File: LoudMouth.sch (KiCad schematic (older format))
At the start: 15 parts, among them P101 CONN_01X02, P102 CONN_01X02, P103 CONN_01X02, Q101 Q_NPN_BCE

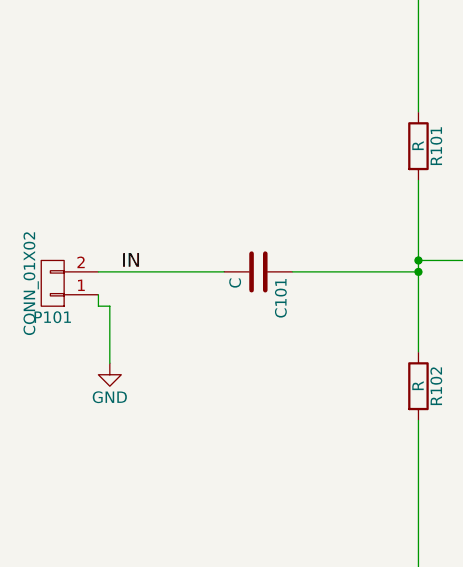
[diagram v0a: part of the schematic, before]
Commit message: Created initial layout and changed input pin config
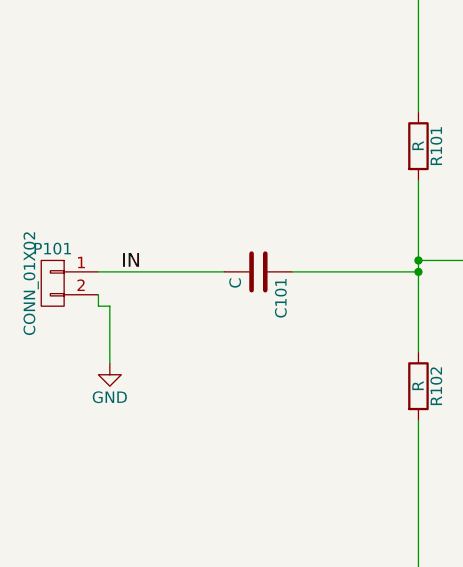
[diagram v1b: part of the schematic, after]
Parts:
- C101, C102, C103, C104: footprint (none) -> Capacitors_SMD:C_1210_HandSoldering
- P101, P102, P103: footprint (none) -> Pin_Headers:Pin_Header_Straight_1x02
- Q101: footprint (none) -> Housings_TO-92:TO-92_Molded_Narrow
- R101, R102, R103, R104, R105, R106, R107: footprint (none) -> Resistors_SMD:R_0805_HandSoldering
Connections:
- net GND: now also P101.2 (P2); no longer P101.1 (P1)
- net IN: now also P101.1 (P1); no longer P101.2 (P2)
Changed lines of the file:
@@
 F 0 "R101" V 4080 2650 50  0000 C CNN
 F 1 "R" V 4000 2650 50  0000 C CNN
-F 2 "" V 3930 2650 30  0000 C CNN
+F 2 "Resistors_SMD:R_0805_HandSoldering" V 3930 2650 30  0001 C CNN
 F 3 "" H 4000 2650 30  0000 C CNN
 	1    4000 2650
@@
 F 0 "R102" V 4080 3700 50  0000 C CNN
 F 1 "R" V 4000 3700 50  0000 C CNN
-F 2 "" V 3930 3700 30  0000 C CNN
+F 2 "Resistors_SMD:R_0805_HandSoldering" V 3930 3700 30  0001 C CNN
 F 3 "" H 4000 3700 30  0000 C CNN
 	1    4000 3700
@@
 F 0 "R104" V 5580 1500 50  0000 C CNN
 F 1 "R" V 5500 1500 50  0000 C CNN
-F 2 "" V 5430 1500 30  0000 C CNN
+F 2 "Resistors_SMD:R_0805_HandSoldering" V 5430 1500 30  0001 C CNN
 F 3 "" H 5500 1500 30  0000 C CNN
 	1    5500 1500
@@
 F 0 "R107" V 5580 4800 50  0000 C CNN
 F 1 "R" V 5500 4800 50  0000 C CNN
-F 2 "" V 5430 4800 30  0000 C CNN
+F 2 "Resistors_SMD:R_0805_HandSoldering" V 5430 4800 30  0001 C CNN
 F 3 "" H 5500 4800 30  0000 C CNN
 	1    5500 4800
@@
 F 0 "C101" H 3325 3300 50  0000 L CNN
 F 1 "C" H 3325 3100 50  0000 L CNN
-F 2 "" H 3338 3050 30  0000 C CNN
+F 2 "Capacitors_SMD:C_1210_HandSoldering" H 3338 3050 30  0001 C CNN
 F 3 "" H 3300 3200 60  0000 C CNN
 	1    3300 3200
@@
 F 0 "C104" H 6175 2400 50  0000 L CNN
 F 1 "C" H 6175 2200 50  0000 L CNN
-F 2 "" H 6188 2150 30  0000 C CNN
+F 2 "Capacitors_SMD:C_1210_HandSoldering" H 6188 2150 30  0001 C CNN
 F 3 "" H 6150 2300 60  0000 C CNN
 	1    6150 2300
@@
 F 0 "C103" H 6075 1600 50  0000 L CNN
 F 1 "C" H 6075 1400 50  0000 L CNN
-F 2 "" H 6088 1350 30  0000 C CNN
+F 2 "Capacitors_SMD:C_1210_HandSoldering" H 6088 1350 30  0001 C CNN
 F 3 "" H 6050 1500 60  0000 C CNN
 	1    6050 1500
@@
 F 0 "C102" H 5875 4900 50  0000 L CNN
 F 1 "C" H 5875 4700 50  0000 L CNN
-F 2 "" H 5888 4650 30  0000 C CNN
+F 2 "Capacitors_SMD:C_1210_HandSoldering" H 5888 4650 30  0001 C CNN
 F 3 "" H 5850 4800 60  0000 C CNN
 	1    5850 4800
@@
 F 0 "Q101" H 5700 3200 50  0000 R CNN
 F 1 "Q_NPN_BCE" H 6000 3100 50  0000 R CNN
-F 2 "" H 5600 3250 29  0000 C CNN
+F 2 "Housings_TO-92:TO-92_Molded_Narrow" H 5600 3250 29  0001 C CNN
 F 3 "" H 5400 3150 60  0000 C CNN
 	1    5400 3150
@@
 F 0 "R103" V 4930 3150 50  0000 C CNN
 F 1 "0" V 4850 3150 50  0000 C CNN
-F 2 "" V 4780 3150 30  0000 C CNN
+F 2 "Resistors_SMD:R_0805_HandSoldering" V 4780 3150 30  0001 C CNN
 F 3 "" H 4850 3150 30  0000 C CNN
 	1    4850 3150
@@
 F 0 "R106" V 5580 3750 50  0000 C CNN
 F 1 "0" V 5500 3750 50  0000 C CNN
-F 2 "" V 5430 3750 30  0000 C CNN
+F 2 "Resistors_SMD:R_0805_HandSoldering" V 5430 3750 30  0001 C CNN
 F 3 "" H 5500 3750 30  0000 C CNN
 	1    5500 3750
@@
 F 0 "R105" V 5580 2550 50  0000 C CNN
 F 1 "0" V 5500 2550 50  0000 C CNN
-F 2 "" V 5430 2550 30  0000 C CNN
+F 2 "Resistors_SMD:R_0805_HandSoldering" V 5430 2550 30  0001 C CNN
 F 3 "" H 5500 2550 30  0000 C CNN
 	1    5500 2550
@@
 F 0 "P101" H 2400 3400 50  0000 C CNN
 F 1 "CONN_01X02" V 2500 3250 50  0000 C CNN
-F 2 "" H 2400 3250 60  0000 C CNN
+F 2 "Pin_Headers:Pin_Header_Straight_1x02" H 2400 3250 60  0001 C CNN
 F 3 "" H 2400 3250 60  0000 C CNN
 	1    2400 3250
-	-1   0    0    1
+	-1   0    0    -1
 $EndComp
 $Comp
@@
 F 0 "P102" H 7100 1400 50  0000 C CNN
 F 1 "CONN_01X02" V 7200 1250 50  0000 C CNN
-F 2 "" H 7100 1250 60  0000 C CNN
+F 2 "Pin_Headers:Pin_Header_Straight_1x02" H 7100 1250 60  0001 C CNN
 F 3 "" H 7100 1250 60  0000 C CNN
 	1    7100 1250
@@
 F 0 "P103" H 7100 2500 50  0000 C CNN
 F 1 "CONN_01X02" V 7200 2350 50  0000 C CNN
-F 2 "" H 7100 2350 60  0000 C CNN
+F 2 "Pin_Headers:Pin_Header_Straight_1x02" H 7100 2350 60  0001 C CNN
 F 3 "" H 7100 2350 60  0000 C CNN
 	1    7100 2350

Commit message: Finished Class A board, ready to send to fab
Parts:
- removed Q101: Q_NPN_BCE, Housings_TO-92:TO-92_Molded_Narrow, symbol Q_NPN_BCE
- added Q101: Q_NPN_EBC, Housings_TO-92:TO-92_Molded_Narrow, symbol Q_NPN_EBC
- added TP101, TP102, TP103: CONN_01X01, Measurement_Points:Measurement_Point_Round-SMD-Pad_Big, symbol CONN_01X01
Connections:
- net IN: now also TP101.1 (P1)
- net OUT: now also TP103.1 (P1)
- net VCC: now also TP102.1 (P1)
- net BASE: now reaches R103.1
- net BASE: now also Q101.2 (B)
- net COLLECTOR: now reaches R105.1
- net COLLECTOR: now also Q101.3 (C)
- net EMITTER: now reaches R106.2
- net EMITTER: now also Q101.1 (E)
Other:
- moved on the sheet: R103
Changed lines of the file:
@@
-$EndComp
-$Comp
-L Q_NPN_BCE Q101
-U 1 1 55F12615
-P 5400 3150
-F 0 "Q101" H 5700 3200 50  0000 R CNN
-F 1 "Q_NPN_BCE" H 6000 3100 50  0000 R CNN
-F 2 "Housings_TO-92:TO-92_Molded_Narrow" H 5600 3250 29  0001 C CNN
-F 3 "" H 5400 3150 60  0000 C CNN
-	1    5400 3150
-	1    0    0    -1
 $EndComp
 $Comp
 L R R103
 U 1 1 55F1265C
-P 4850 3150
-F 0 "R103" V 4930 3150 50  0000 C CNN
-F 1 "0" V 4850 3150 50  0000 C CNN
-F 2 "Resistors_SMD:R_0805_HandSoldering" V 4780 3150 30  0001 C CNN
-F 3 "" H 4850 3150 30  0000 C CNN
-	1    4850 3150
+P 4650 3150
+F 0 "R103" V 4730 3150 50  0000 C CNN
+F 1 "0" V 4650 3150 50  0000 C CNN
+F 2 "Resistors_SMD:R_0805_HandSoldering" V 4580 3150 30  0001 C CNN
+F 3 "" H 4650 3150 30  0000 C CNN
+	1    4650 3150
 	0    1    1    0
 $EndComp
@@
 $EndComp
 $Comp
-L GND #PWR01
+L GND #PWR101
 U 1 1 55F12AAF
 P 2650 3600
-F 0 "#PWR01" H 2650 3350 50  0001 C CNN
+F 0 "#PWR101" H 2650 3350 50  0001 C CNN
 F 1 "GND" H 2650 3450 50  0000 C CNN
 F 2 "" H 2650 3600 60  0000 C CNN
@@
 $EndComp
 $Comp
-L GND #PWR02
+L GND #PWR102
 U 1 1 55F12D58
 P 5500 5200
-F 0 "#PWR02" H 5500 4950 50  0001 C CNN
+F 0 "#PWR102" H 5500 4950 50  0001 C CNN
 F 1 "GND" H 5500 5050 50  0000 C CNN
 F 2 "" H 5500 5200 60  0000 C CNN
@@
 $EndComp
 $Comp
-L GND #PWR03
+L GND #PWR105
 U 1 1 55F12DBD
 P 6850 2600
-F 0 "#PWR03" H 6850 2350 50  0001 C CNN
+F 0 "#PWR105" H 6850 2350 50  0001 C CNN
 F 1 "GND" H 6850 2450 50  0000 C CNN
 F 2 "" H 6850 2600 60  0000 C CNN
@@
 $EndComp
 $Comp
-L GND #PWR04
+L GND #PWR104
 U 1 1 55F12E4F
 P 6850 1450
-F 0 "#PWR04" H 6850 1200 50  0001 C CNN
+F 0 "#PWR104" H 6850 1200 50  0001 C CNN
 F 1 "GND" H 6850 1300 50  0000 C CNN
 F 2 "" H 6850 1450 60  0000 C CNN
@@
 	6850 1300 6850 1450
 Wire Wire Line
-	6900 2300 6300 2300
+	6300 2300 6900 2300
 Wire Wire Line
 	6900 2400 6850 2400
@@
 Connection ~ 6050 1200
 $Comp
-L GND #PWR05
+L GND #PWR103
 U 1 1 55F12F56
 P 6050 1750
-F 0 "#PWR05" H 6050 1500 50  0001 C CNN
+F 0 "#PWR103" H 6050 1500 50  0001 C CNN
 F 1 "GND" H 6050 1600 50  0000 C CNN
 F 2 "" H 6050 1750 60  0000 C CNN
@@
 	5500 2700 5500 2950
 Wire Wire Line
-	5200 3150 5000 3150
+	5200 3150 4800 3150
 Wire Wire Line
 	5500 3350 5500 3600
@@
 Connection ~ 5500 5100
 Wire Wire Line
-	4700 3150 4000 3150
+	4500 3150 4000 3150
 Connection ~ 4000 3150
 Wire Wire Line
@@
 Wire Wire Line
 	4000 1200 4000 2500
+$Comp
+L CONN_01X01 TP101
+U 1 1 55F1613F
+P 2950 2800
+F 0 "TP101" H 2950 2900 50  0000 C CNN
+F 1 "CONN_01X01" V 3050 2800 50  0000 C CNN
+F 2 "Measurement_Points:Measurement_Point_Round-SMD-Pad_Big" H 2950 2800 60  0001 C CNN
+F 3 "" H 2950 2800 60  0000 C CNN
+	1    2950 2800
+	0    -1   -1   0
+$EndComp
+Wire Wire Line
+	2950 3000 2950 3200
+Connection ~ 2950 3200
+$Comp
+L CONN_01X01 TP102
+U 1 1 55F162D1
+P 6300 800
+F 0 "TP102" H 6300 900 50  0000 C CNN
+F 1 "CONN_01X01" V 6400 800 50  0000 C CNN
+F 2 "Measurement_Points:Measurement_Point_Round-SMD-Pad_Big" H 6300 800 60  0001 C CNN
+F 3 "" H 6300 800 60  0000 C CNN
+	1    6300 800
+	0    -1   -1   0
+$EndComp
+Wire Wire Line
+	6300 1000 6300 1200
+Connection ~ 6300 1200
+$Comp
+L CONN_01X01 TP103
+U 1 1 55F1666E
+P 6400 1900
+F 0 "TP103" H 6400 2000 50  0000 C CNN
+F 1 "CONN_01X01" V 6500 1900 50  0000 C CNN
+F 2 "Measurement_Points:Measurement_Point_Round-SMD-Pad_Big" H 6400 1900 60  0001 C CNN
+F 3 "" H 6400 1900 60  0000 C CNN
+	1    6400 1900
+	0    -1   -1   0
+$EndComp
+Wire Wire Line
+	6400 2100 6400 2300
+Connection ~ 6400 2300
+Text Label 4900 3150 0    60   ~ 0
+BASE
+Text Label 5500 3500 0    60   ~ 0
+EMITTER
+Text Label 5500 2800 0    60   ~ 0
+COLLECTOR
+$Comp
+L Q_NPN_EBC Q101
+U 1 1 55F17610
+P 5400 3150
+F 0 "Q101" H 5700 3200 50  0000 R CNN
+F 1 "Q_NPN_EBC" H 6000 3100 50  0000 R CNN
+F 2 "Housings_TO-92:TO-92_Molded_Narrow" H 5600 3250 29  0001 C CNN
+F 3 "" H 5400 3150 60  0000 C CNN
+	1    5400 3150
+	1    0    0    -1
+$EndComp
 $EndSCHEMATC
